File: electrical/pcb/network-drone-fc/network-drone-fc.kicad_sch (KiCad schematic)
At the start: 57 parts, among them J1 U.FL-R-SMT-1, J2 TYPE-C 16PIN 2MD, SW1 RESET, SW2 BOOT, U1 ESP32-S3FN8, U2 USBLC6-2SC6, U3 AP63205WU-7, U4 TLV75733PDBVR, U5 TPS7A2033PDBVR, X1 Q22FA12800101

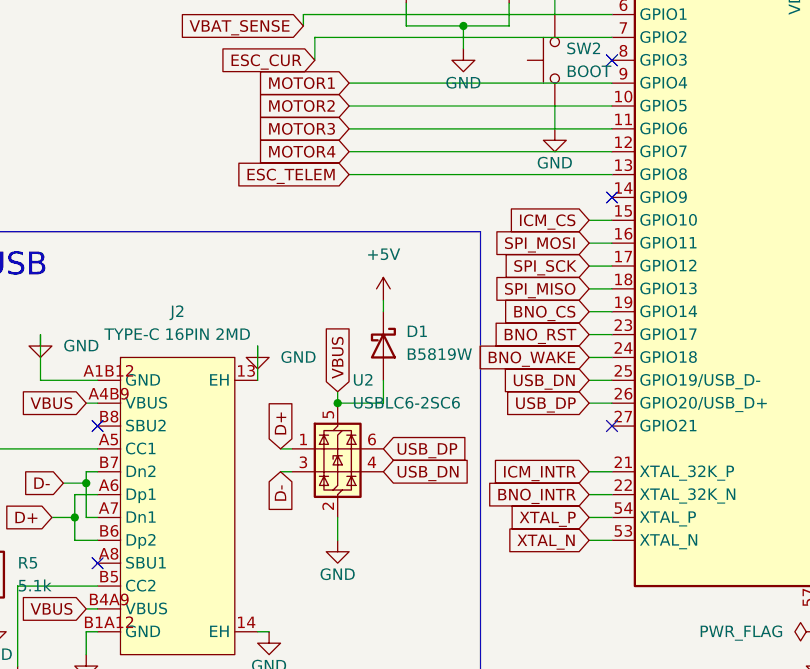
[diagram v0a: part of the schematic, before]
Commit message: Schematic: remove BNO085 labels, move ESC_TELEM to GPIO17, add DOCK_DET and AUX_ADC labels
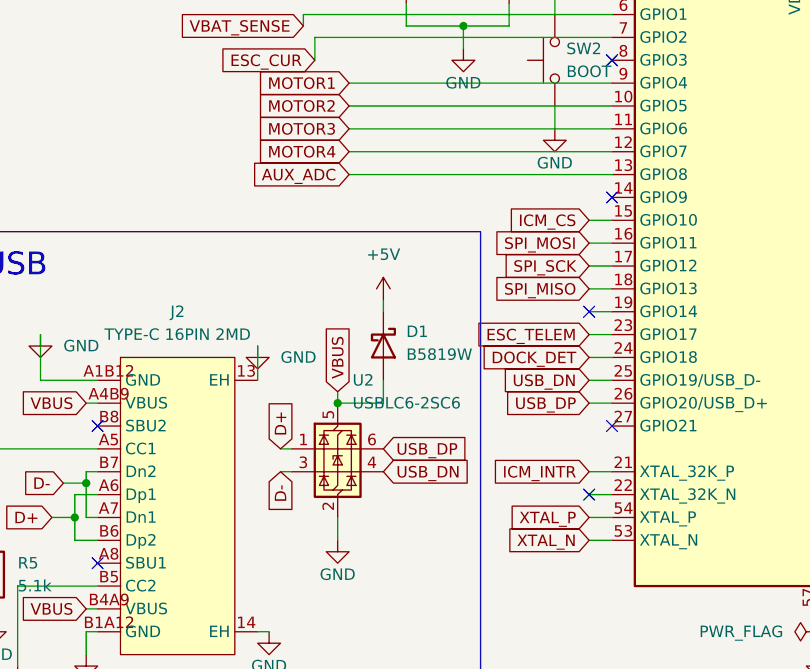
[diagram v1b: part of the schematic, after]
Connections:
- net BNO_RST is gone; now on net ESC_TELEM: U1.23 (GPIO17)
- net ESC_TELEM: no longer U1.13 (GPIO8)
- net BNO_CS: no longer names the net of U1.19 (GPIO14)
- net BNO_INTR: no longer names the net of U1.22 (XTAL_32K_N)
- net BNO_WAKE renamed DOCK_DET
- new net AUX_ADC: U1.13 (GPIO8)
- no-connect marks 20 -> 22

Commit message: Schematic: wire ICM-42688-P IMU on SPI with INT1/INT2 and CS pull-up
BMP581 and MAX-M10S are placed but not wired yet.
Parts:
- added C25: 0.1uF, symbol Device:C
- added C26: 2.2uF, symbol Device:C
- added C27: 10nF, symbol Device:C
- added R11: 10K, symbol Device:R
- added U6: ICM-42688-P, tar_fc:LGA-14_L3.0-W2.5-P0.50-TL, symbol tar_fc:ICM-42688-P
- added U7: BMP581, tar_fc:LGA-10_L2.0-W2.0-P0.50-TL_BMP581, symbol tar_fc:BMP581
- added U8: MAX-M10S-00B, tar_fc:SMD-18_L10.1-W9.7-P1.10-TL_SKG09F, symbol tar_fc:MAX-M10S-00B
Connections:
- net +3V3_SENS: now also C25.1, C26.2, C27.2, R11.1, U6.5 (VDDIO), U6.8 (VDD)
- net GND: now also C25.2, C26.1, C27.1, U6.11 (RESV), U6.6 (GND), U6.7 (RESV)
- net ICM_CS: now also R11.2, U6.12 (AP_CS)
- net ICM_INTR: now also U6.4 (INT1/INT)
- net SPI_MISO: now also U6.1 (AP_SDO/AP_AD0)
- net SPI_MOSI: now also U6.14 (AP_SDA/AP_SDIO/AP_SDI)
- net SPI_SCK: now also U6.13 (AP_SCL/AP_SCLK)
- net ICM_INT2: now reaches U1.14 (GPIO9)
- net ICM_INT2: now also U6.9 (INT2/FSYNC/CLKIN)
- no-connect marks 22 -> 24

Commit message: Schematic: complete sensors and connectors boxes, assign all footprints
BMP581 on I2C (CSB high, SDO low, 4.7k pull-ups), MAX-M10S GPS with U.FL and
a DNP bias-T for an active antenna, ESC JST-SH 8 (Betaflight pin order), I2C
and UART JST-GH ports (Dronecode order), charging-board port (DOCK_DET,
AUX_ADC). ESP32 power-pin decoupling redrawn as one rail with the LC filter,
IMU VDDIO capacitor moved off the pin-7 ground stub. ERC: 0 errors, 0 warnings.
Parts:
- added C28, C29, C31, C33, C34: 100nF, Capacitor_SMD:C_0402_1005Metric, symbol Device:C
- added C30: 10uF, Capacitor_SMD:C_0603_1608Metric, symbol Device:C
- added C32: 10nF, Capacitor_SMD:C_0402_1005Metric, symbol Device:C
- added J3: U.FL GPS, tar_fc:RF-SMD_FRF05002-JSS103M, symbol tar_fc:U.FL-R-SMT-1
- added J4: ESC, tar_fc:CONN-TH_SM08B-SRSS-TB-LF-SN, symbol tar_fc:SM08B-SRSS-TB
- added J5: I2C port, tar_fc:CONN-SMD_4P-P1.25_SM04B-GHS-TB-LF-SN, symbol tar_fc:SM04B-GHS-TB
- added J6: UART port, tar_fc:CONN-SMD_4P-P1.25_SM04B-GHS-TB-LF-SN, symbol tar_fc:SM04B-GHS-TB
- added J7: Charging board, tar_fc:CONN-SMD_4P-P1.25_SM04B-GHS-TB-LF-SN, symbol tar_fc:SM04B-GHS-TB
- added L3: 27nH DNP, Inductor_SMD:L_0402_1005Metric, symbol Device:L
- added R12, R13: 4.7k, Resistor_SMD:R_0402_1005Metric, symbol Device:R
- C1, C10, C11, C12, C13, C14, C15, C17, C2, C20, C21, C22, C23, C24, C25, C26, C27, C3, C5, C6, C7, C8, C9: footprint (none) -> Capacitor_SMD:C_0402_1005Metric
- C16: footprint (none) -> Capacitor_SMD:C_0805_2012Metric
- C18, C19: value 22uF -> 22uF 10V; footprint (none) -> Capacitor_SMD:C_0805_2012Metric
- C4: value 10uF -> 10uF 6.3V; footprint (none) -> Capacitor_SMD:C_0603_1608Metric
- D1: footprint (none) -> Diode_SMD:D_SOD-123
- D2, D3, D4: footprint (none) -> LED_SMD:LED_0603_1608Metric
- L1: footprint (none) -> Inductor_SMD:L_0402_1005Metric
- L2: footprint (none) -> Inductor_SMD:L_1008_2520Metric
- R1, R10, R2, R3, R4, R5, R6, R7, R8, R9: footprint (none) -> Resistor_SMD:R_0402_1005Metric
- R11: value 10K -> 10k; footprint (none) -> Resistor_SMD:R_0402_1005Metric
- SW1, SW2: footprint (none) -> Button_Switch_SMD:SW_SPST_PTS810
- TP1, TP2, TP3, TP4, TP5, TP6: footprint (none) -> TestPoint:TestPoint_Pad_D1.0mm
- U7: LCSC (none) -> C5362283; LCSC Part C5362283 -> (none); MPN BMP581 -> (none); Manufacturer Bosch(博世) -> (none)
- U8: value MAX-M10S-00B -> MAX-M10S; LCSC (none) -> C4153167; LCSC Part C4153167 -> (none); MPN MAX-M10S-00B -> (none); Manufacturer U-BLOX(优北罗) -> (none)
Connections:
- net +3V3: now also J5.1
- net +3V3_SENS: now also C27.1, U7.1 (VDDIO), U7.10 (VDD), U7.6 (CSB), U8.7 (V_IO), U8.8 (VCC), C28.1, C29.1, C30.1, C31.1, R12.1, R13.1; no longer C27.2
- net +5V: now also J6.1
- net AUX_ADC: now also C34.1, J7.3
- net DOCK_DET: now also J7.2
- net ESC_CUR: now also C33.1, J4.3
- net ESC_TELEM: now also J4.4
- net GND: now also C27.2, U7.3 (VSS), U7.5 (SDO), U7.8 (VSS), U7.9 (VSS), U8.1 (GND), U8.10 (GND), U8.12 (GND), C28.2, C29.2, C30.2, C31.2, C32.2, C33.2, C34.2, J3.2 (GND), J3.3 (GND), J4.1, J5.4, J6.4, J7.1; no longer C27.1
- net GPS_RX: now also U8.2 (TXD)
- net GPS_TX: now also U8.3 (RXD)
- net I2C_SCL: now also U7.2 (SCK), J5.2, R13.2
- net I2C_SDA: now also U7.4 (SDI), J5.3, R12.2
- net MOTOR1: now also J4.5
- net MOTOR2: now also J4.6
- net MOTOR3: now also J4.7
- net MOTOR4: now also J4.8
- net UART_RX: now also J6.3
- net UART_TX: now also J6.2
- net VBAT: now also J4.2
- net at U8.11 (RF_IN): now also J3.1 (SIG), L3.2
- net at U8.14 (VCC_RF): now also C32.1, L3.1
- no-connect marks 24 -> 43
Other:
- note added: "Barometer"
- note added: "CSB high = I2C mode, SDO low = address 0x46"
- note added: "ESC (JST-SH 8)"
- note added: "GPS"
- note added: "I2C and UART ports use the Dronecode order: VCC, SCL/TX, SDA/RX, GND. Charging port: GND, DOCK_DET, AUX_ADC, spare."
- note added: "IMU"
- note added: "L3 only for an active antenna (bias-T). RF_IN is DC-blocked internally; keep the trace 50 ohm."
- note added: "Pin order follows the Betaflight 4-in-1 standard: GND, VBAT, CUR, TLM, M1-M4. Confirm against the ESC."
- note added: "Ports (JST-GH 4)"
- moved on the sheet: C25, C26, R11, U6

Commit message: PCB: place every part on the 36x36 board, nets from the schematic, rules set
All parts on the top side per the floorplan: IMU centre, ESP32 right with its
decoupling column and crystal, GPS top with its U.FL at the corner, buck above
the ESC connector, ports on the edges, test pads on the bottom. Plain NPTH M2
holes. DRC: no clearance, edge or courtyard errors; routing still to do.
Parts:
- D5: footprint Diode_SMD:D_SMA -> tar_fc:SMA_L4.4-W2.6-LS5.0-RD
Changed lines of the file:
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@@
 			)
 		)
-		(property "Footprint" "Diode_SMD:D_SMA"
+		(property "Footprint" "tar_fc:SMA_L4.4-W2.6-LS5.0-RD"
 			(at 124.46 46.99 0)
 			(effects

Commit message: Pads instead of buttons, twelve more test points, 3 mm hole keep-out
RESET/BOOT become JP1/JP2 solder-jumper pad pairs on the bottom. TP7-TP18 bring
the IMU SPI bus, I2C, GPS UART, ESC telemetry and the spare UART to bottom-side
pads. The spare UART connector J6 is dropped: with 3 mm clear around each hole
for grommets, the board has one connector slot per edge. Charging port moves to
the top right. DRC: no copper errors.
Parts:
- removed J6: UART port, tar_fc:CONN-SMD_4P-P1.25_SM04B-GHS-TB-LF-SN, symbol tar_fc:SM04B-GHS-TB
- added TP10, TP11, TP12, TP13, TP14, TP15, TP16, TP17, TP18, TP7, TP8, TP9: TestPoint, TestPoint:TestPoint_Pad_D1.0mm, symbol Connector:TestPoint
- JP1: renamed from SW1; footprint Button_Switch_SMD:SW_SPST_PTS810 -> Jumper:SolderJumper-2_P1.3mm_Open_RoundedPad1.0x1.5mm; symbol Switch:SW_Push -> Jumper:SolderJumper_2_Open
- JP2: renamed from SW2; footprint Button_Switch_SMD:SW_SPST_PTS810 -> Jumper:SolderJumper-2_P1.3mm_Open_RoundedPad1.0x1.5mm; symbol Switch:SW_Push -> Jumper:SolderJumper_2_Open
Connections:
- net ESC_TELEM: now also TP16.1
- net GPS_RX: now also TP15.1
- net GPS_TX: now also TP14.1
- net I2C_SCL: now also TP13.1
- net I2C_SDA: now also TP12.1
- net ICM_CS: now also TP10.1
- net ICM_INTR: now also TP11.1
- net SPI_MISO: now also TP9.1
- net SPI_MOSI: now also TP8.1
- net SPI_SCK: now also TP7.1
- net UART_RX: now also TP18.1
- net UART_TX: now also TP17.1
- no-connect marks 43 -> 41
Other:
- note added: "Bottom-side pads for probing the buses and recovering the ESP32.\nShort the RESET or BOOT pad pair to GND with tweezers."
- note added: "I2C port uses the Dronecode order: VCC, SCL, SDA, GND. The spare UART is on test pads TP17/TP18. Charging port: GND, DOCK_DET, AUX_ADC, spare."
- note added: "Test points"
- note removed: "I2C and UART ports use the Dronecode order: VCC, SCL/TX, SDA/RX, GND. Charging port: GND, DOCK_DET, AUX_ADC, spare."

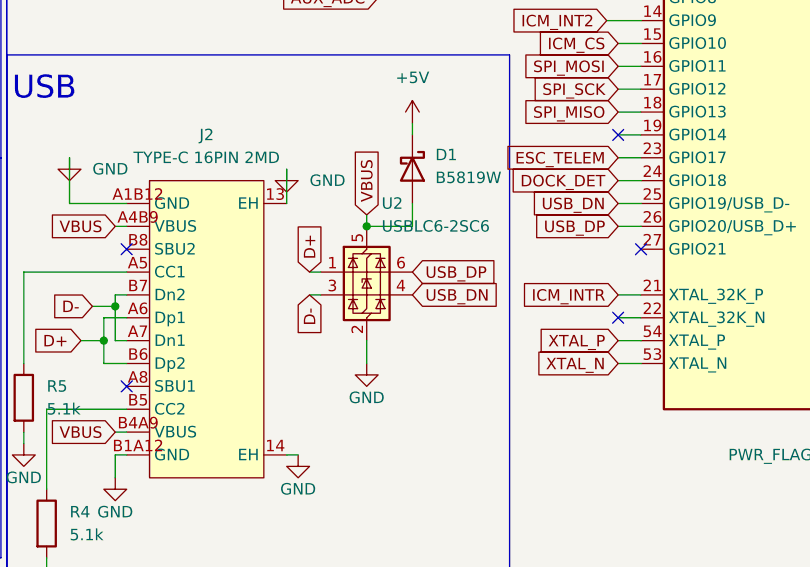
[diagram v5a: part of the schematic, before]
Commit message: PCB: placement reworked for routing; antenna, GPS feed, crystal, USB and buck routed by hand
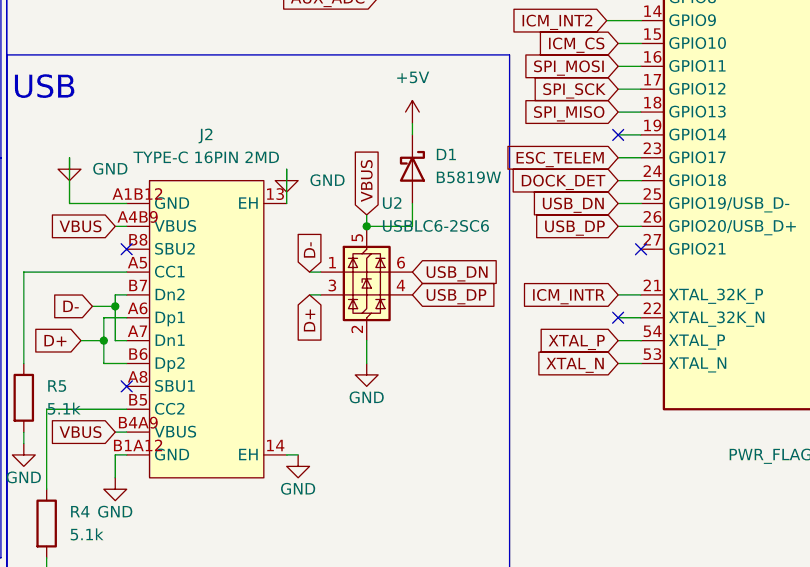
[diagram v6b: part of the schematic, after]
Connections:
- net D+: now also U2.3 (I/O2); no longer U2.1 (I/O1)
- net D-: now also U2.1 (I/O1); no longer U2.3 (I/O2)
- net USB_DN: now also U2.6 (I/O1); no longer U2.4 (I/O2)
- net USB_DP: now also U2.4 (I/O2); no longer U2.6 (I/O1)

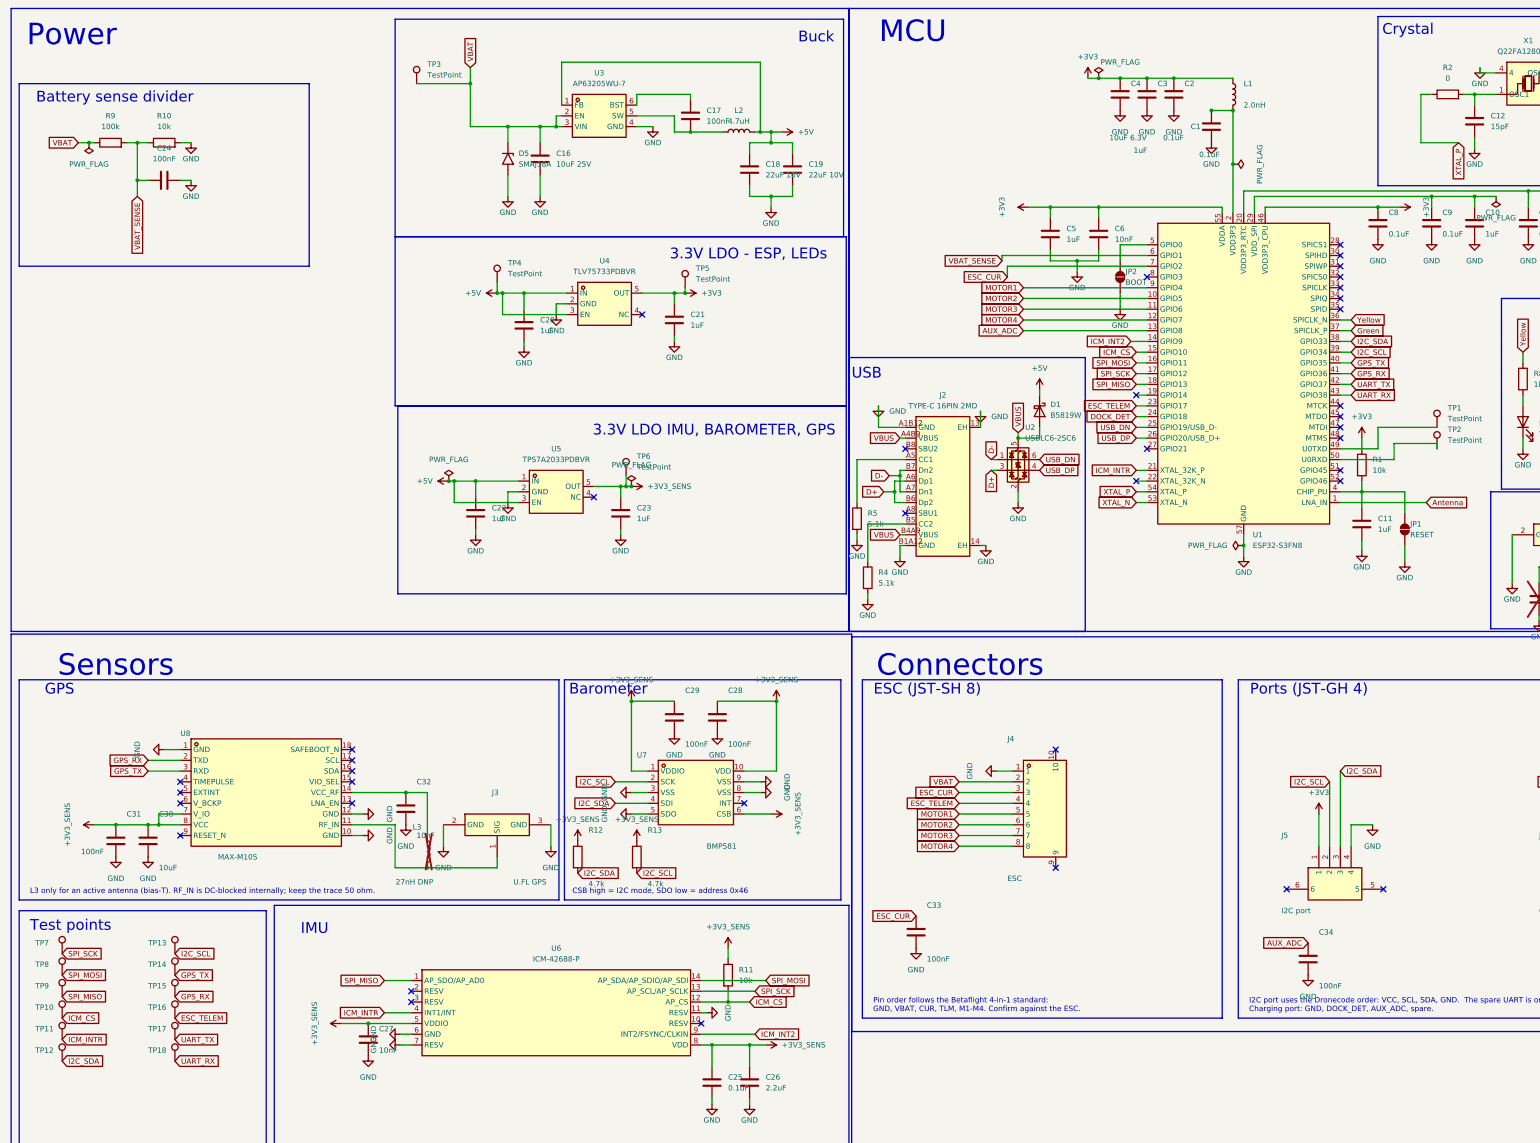
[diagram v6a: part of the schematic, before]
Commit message: Schematic: ESP32 re-pinned for routing; INT2, R2 and eleven test pads dropped
Motors on GPIO11/13/16/6, ESC telemetry GPIO10, battery sense GPIO4, dock detect GPIO9, GPS UART GPIO18/36, IMU SPI on GPIO33/34/35/47/48, I2C on GPIO37/38, LEDs on GPIO39/40. The IMU's INT2/FSYNC pin is left open, the 0 ohm XTAL_P jumper R2 is gone, and only seven test pads remain (UART0, the four rails, I2C SCL). ERC 0 errors, 0 warnings.
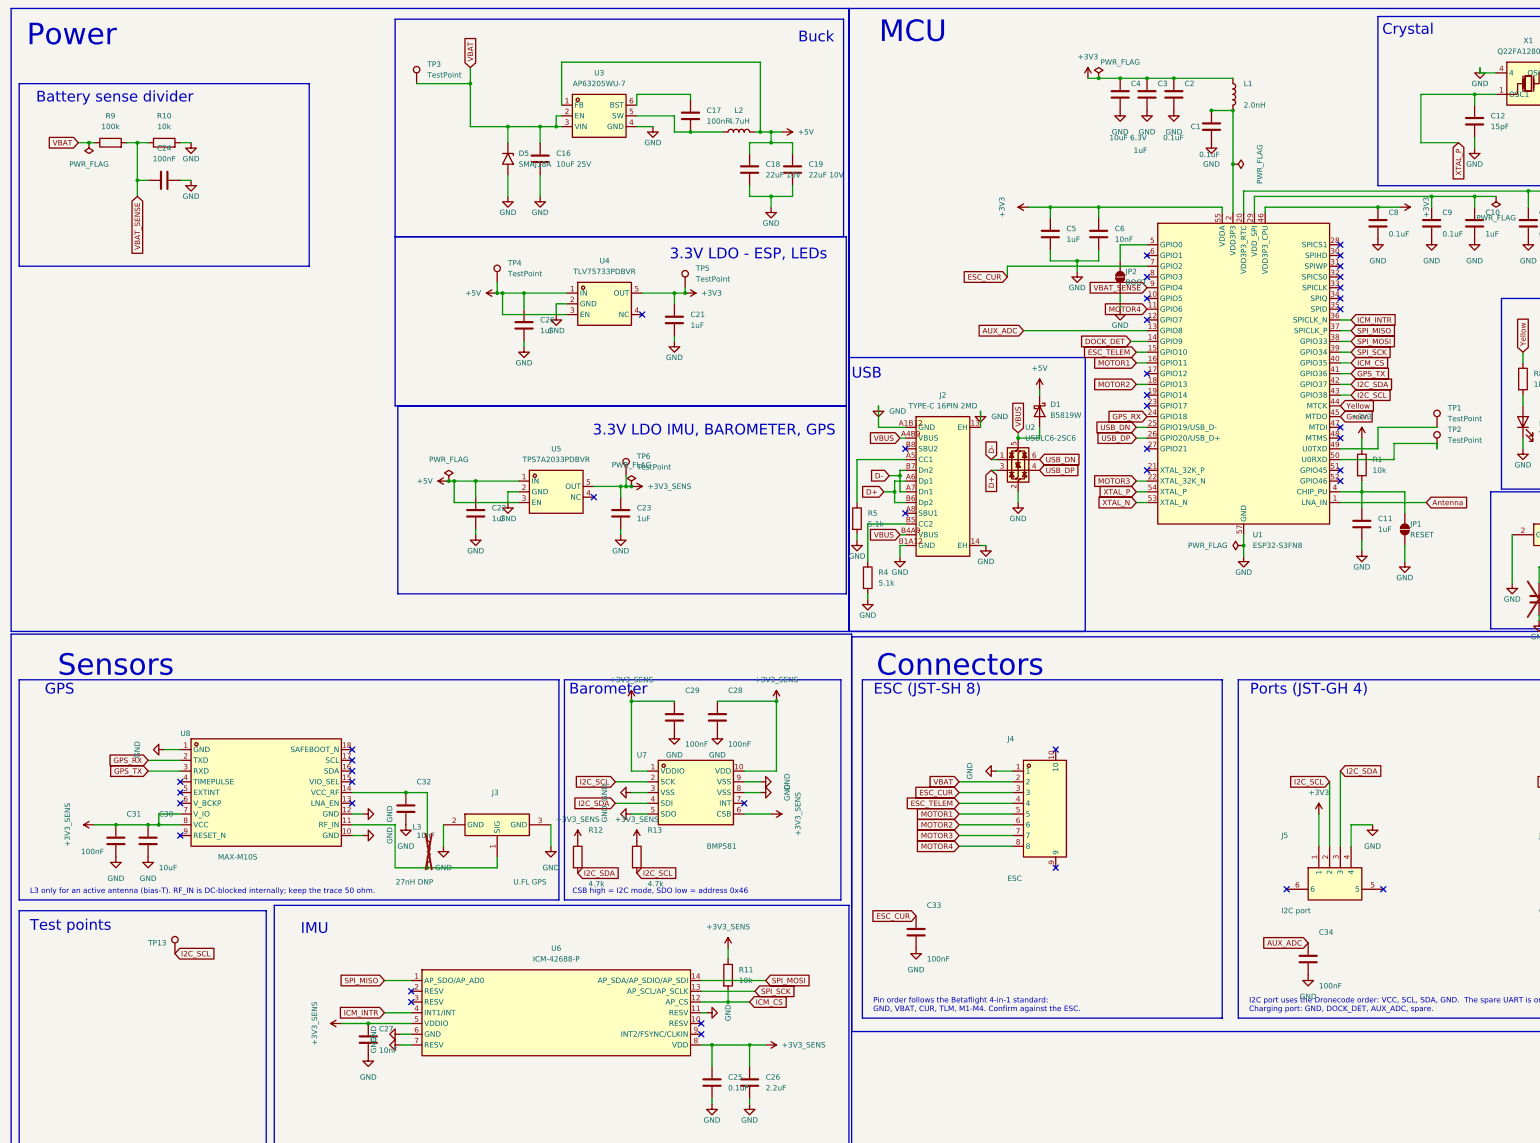
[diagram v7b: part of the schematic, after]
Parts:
- removed R2: 0, Resistor_SMD:R_0402_1005Metric, symbol Device:R
- removed TP10, TP11, TP12, TP14, TP15, TP16, TP17, TP18, TP7, TP8, TP9: TestPoint, TestPoint:TestPoint_Pad_D1.0mm, symbol Connector:TestPoint
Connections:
- net UART_RX is gone; now on net I2C_SCL: U1.43 (GPIO38)
- net UART_TX is gone; now on net I2C_SDA: U1.42 (GPIO37)
- net DOCK_DET: now also U1.14 (GPIO9); no longer U1.24 (GPIO18)
- net ESC_TELEM: now also U1.15 (GPIO10); no longer U1.23 (GPIO17)
- net GPS_RX: now also U1.24 (GPIO18); no longer U1.41 (GPIO36)
- net GPS_TX: now also U1.41 (GPIO36); no longer U1.40 (GPIO35)
- net Green: now also U1.45 (MTDO); no longer U1.37 (SPICLK_P)
- net I2C_SCL: no longer U1.39 (GPIO34)
- net I2C_SDA: no longer U1.38 (GPIO33)
- net ICM_CS: now also U1.40 (GPIO35); no longer U1.15 (GPIO10)
- net ICM_INTR: now also U1.36 (SPICLK_N); no longer U1.21 (XTAL_32K_P)
- net MOTOR1: now also U1.16 (GPIO11); no longer U1.9 (GPIO4)
- net MOTOR2: now also U1.18 (GPIO13); no longer U1.10 (GPIO5)
- net MOTOR3: now also U1.22 (XTAL_32K_N); no longer U1.11 (GPIO6)
- net MOTOR4: now also U1.11 (GPIO6); no longer U1.12 (GPIO7)
- net SPI_MISO: now also U1.37 (SPICLK_P); no longer U1.18 (GPIO13)
- net SPI_MOSI: now also U1.38 (GPIO33); no longer U1.16 (GPIO11)
- net SPI_SCK: now also U1.39 (GPIO34); no longer U1.17 (GPIO12)
- net VBAT_SENSE: now also U1.9 (GPIO4); no longer U1.6 (GPIO1)
- net XTAL_P: now also C12.1, X1.1 (OSC1)
- net Yellow: now also U1.44 (MTCK); no longer U1.36 (SPICLK_N)
- net ICM_INT2: no longer names the net of U6.9 (INT2/FSYNC/CLKIN)
- net ICM_INT2: no longer U1.14 (GPIO9)
- no-connect marks 41 -> 45

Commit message: Schematic: drop the spare-UART note from the connector sheet
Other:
- note added: "I2C port uses the Dronecode order: VCC, SCL, SDA, GND. Charging port: GND, DOCK_DET, AUX_ADC, spare."
- note removed: "I2C port uses the Dronecode order: VCC, SCL, SDA, GND. The spare UART is on test pads TP17/TP18. Charging port: GND, DOCK_DET, AUX_ADC, spare."
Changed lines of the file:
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@@
 		)
 	)
-	(text "I2C port uses the Dronecode order: VCC, SCL, SDA, GND.  The spare UART is on test pads TP17/TP18.\nCharging port: GND, DOCK_DET, AUX_ADC, spare."
+	(text "I2C port uses the Dronecode order: VCC, SCL, SDA, GND.\nCharging port: GND, DOCK_DET, AUX_ADC, spare."
 		(exclude_from_sim no)
 		(at 304.8 248.92 0)
